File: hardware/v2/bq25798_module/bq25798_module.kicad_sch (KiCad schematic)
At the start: 54 parts, among them IC1 BQ25798RQMR, J1 Input 12V DC, J2 Output 12V DC, J3 Battery, J5 I2C (no pullups), J6 NTC temp sensor, Q1 AON7528, Q2 AON7528

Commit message: update board to v2.1
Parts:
- removed JP6: Temp simul, Jumper:SolderJumper-2_P1.3mm_Bridged_RoundedPad1.0x1.5mm, symbol Jumper:SolderJumper_2_Bridged
- removed NT3: ~, NetTie:NetTie-2_SMD_Pad0.5mm, symbol Device:NetTie_2
- removed TP1: TS, TestPoint:TestPoint_Loop_D1.80mm_Drill1.0mm_Beaded, symbol Connector:TestPoint
- added C23: 47n 25V, Capacitor_SMD:C_0402_1005Metric, symbol Device:C
- added D2: LED, LED_SMD:LED_1206_3216Metric, symbol Device:LED
- added J4: I2C, Connector_JST:JST_XH_B3B-XH-A_1x03_P2.50mm_Vertical, symbol Connector:Conn_01x03_Pin
- C1, C2: value 47n 10V -> 47n 25V; Parameters 10V X7R -> X7R; Source https://www.tme.eu/cz/details/grm155r71a473ka01d/kondenzato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 -> https://www.tme.eu/cz/details/gcm155r71e473ka55d/kondenzato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
- C10, C11, C12, C13, C14, C15, C16, C17, C18, C19, C21, C4: value 10u -> 10u 25V; Parameters 25V X5R -> X7R; Source https://www.tme.eu/cz/details/grm319r6ya106ka12d/kondenzato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 -> https://www.tme.eu/cz/details/grm31cr71e106ka12l/kondenzato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
- C20, C22, D1, L1: Bought basket @TME -> (none)
- C3: value 4.7u -> 4.7u 10V; footprint Capacitor_SMD:C_0805_2012Metric -> Capacitor_SMD:C_1206_3216Metric; Bought at home -> basket @TME; Parameters 25V X5R -> X7R; Source https://www.laskakit.cz/samsung-cl21a475kaqnnne-0805-4-7uf-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 -> https://www.tme.eu/cz/details/grm31cr71e106ka12l/kondenzato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; now fitted; now in the parts list
- C5, C6, C7, C9: value 100n -> 100n 25V; Parameters 50V X7R -> X7R; Source https://www.tme.eu/cz/details/c1005x7r1h104kbb/kondenzatory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 -> https://www.tme.eu/cz/details/gcm155r71e104ke02d/kondenzato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
- C8: value 1nF, 50V, 0402 package -> 1nF, 50V; Parameters 50V X7R -> X7R; Source https://www.tme.eu/cz/details/0402b102k500ct/kondenzatory-m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 -> https://www.tme.eu/cz/details/04023c102kat2a/kondenzatory-m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
- IC1: Bought bought @Ali -> bought @TI
- J5: value I2C (no pullups) -> I2C QWIIC/uŠup; Bought basket @TME -> (none)
- J6: footprint Connector_PinSocket_2.54mm:PinSocket_1x02_P2.54mm_Vertical -> Connector_JST:JST_XH_B2B-XH-A_1x02_P2.50mm_Vertical
- NT1: value grounds -> ~
- R1, R4, R5, R6, R7: Bought at home -> (none)
- R2: value 127k -> 1R; now fitted; now in the parts list
- R3: value 100k -> 1M; now fitted; now in the parts list
- R8: value ? -> 2k2; Bought (none) -> (none); now fitted
- R9: Parameters Do not populate if NTC is used -> (none)
- TP3: value GND -> PGND
- TP6: value Charge status (OD) -> STAT
- TP7: value Interrupt (OD) -> INT
- TP8: value REGN LDO -> REGN
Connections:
- net GND: now also J6.1 (Pin_1), J4.1 (Pin_1); no longer C8.2, IC1.10 (ACDRV2), IC1.13 (~{CE}), J6.2 (Pin_2), TP3.1
- net I2C_SCL: now also J4.3 (Pin_3)
- net I2C_SDA: now also J4.2 (Pin_2)
- net PGND: now also C8.2, IC1.10 (ACDRV2), TP3.1, C23.2
- net REGN: now also R6.1, R8.1
- net STAT: now also D2.1 (K)
- net TS: now also J6.2 (Pin_2); no longer J6.1 (Pin_1), R8.1, R9.2
- net at R8.2: now also D2.2 (A); no longer R6.1
- net at IC1.18 (BATP), R4.1: now also C23.1
- new net: IC1.13 (~{CE}), R9.2
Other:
- note added: "Controller connectors"
- note added: "Grounds"
- note added: "PGND = power ground (thicker traces, special net on PCB) GND = digital ground (ordinary traces) PWR_FLAGs are for DRC in PCB editor."
- note added: "RESET pin?"
- note removed: "255k = 500mA 127k = 1500 mA 0R = max current"
- note removed: "5,89 * REGN = normal temp"
- note removed: "Configure default switching frequency and cell count 27k = 750 kHz + 4 cells"
- note removed: "I2C connector"
- note removed: "Input current limit"
- note removed: "Simulate thermal state: 10k = normal 4.87k = warm 0R = hot"
- note removed: "Simulate thermal state: inf = normal 7.68k = cool 0R = cold"
- title: (none) -> BQ25798 UPS module
- moved on the sheet: C1, C10, C11, C12, C13, C14, C15, C16, C17, C18, C19, C2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

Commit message: wip
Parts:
- removed J5: I2C QWIIC/uŠup, Connector_JST:JST_SH_BM04B-SRSS-TB_1x04-1MP_P1.00mm_Vertical, symbol Connector:Conn_01x04_Pin
- added C24, C25: 47u low ESR, Capacitor_SMD:C_Elec_6.3x5.8, symbol Device:C_Polarized
- C10, C11, C12, C13, C14, C15, C16, C17, C18, C19, C21, C4: footprint Capacitor_SMD:C_1206_3216Metric -> Capacitor_SMD:C_0805_2012Metric; Source https://www.tme.eu/cz/details/grm31cr71e106ka12l/kondenzato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 -> https://www.tme.eu/cz/details/grj21br61e106ke01k/kondenzato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
- C23: Bought (none) -> basket @TME; Parameters 50V X7R -> X7R; Source https://www.tme.eu/cz/details/c1005x7r1h104kbb/kondenzatory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 -> https://www.tme.eu/cz/details/gcm155r71e473ka55d/kondenzato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
- C3: footprint Capacitor_SMD:C_1206_3216Metric -> Capacitor_SMD:C_0805_2012Metric; Source https://www.tme.eu/cz/details/grm31cr71e106ka12l/kondenzato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 -> https://www.tme.eu/cz/details/grm21br71e475ka73l/kondenzato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
- C8: Source https://www.tme.eu/cz/details/04023c102kat2a/kondenzatory-m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 -> https://www.tme.eu/cz/details/gcm1555c1h102ja16d/kondenzato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
- D1: Bought (none) -> ?? nemám je doma?
- D2, J4: Bought (none) -> at home
- L1: footprint snapeda:INDM7676X435N -> Inductor_SMD:L_12x12mm_H6mm; Bought (none) -> basket @TME; Parameters 7.06A I_sat -> >7.06A I_sat; Source https://www.tme.eu/cz/en/details/dr74-2r2-r/smd-power-induc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 -> https://www.tme.eu/cz/details/dr125-2r2-r/tlumivky/eaton-el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
- R3: Bought at home -> (none)
- R5: Parameters MEASURE CHECK!!! -> (none)
- R9: Bought at home -> basket @TME; Parameters (none) -> doplnění zásob; Source (none) -> https://www.tme.eu/cz/en/details/rt0805brd0710k/smd-resisto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
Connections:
- net PGND: now also C24.2, C25.2
- net PMID: now also C24.1, C25.1
- no-connect marks 4 -> 3
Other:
- note added: "?? nestacil by bezny?"
- moved on the sheet: J4

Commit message: v2.1 final
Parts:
- removed J4: I2C, Connector_JST:JST_XH_B3B-XH-A_1x03_P2.50mm_Vertical, symbol Connector:Conn_01x03_Pin
- removed TP6: STAT, TestPoint:TestPoint_Loop_D1.80mm_Drill1.0mm_Beaded, symbol Connector:TestPoint
- removed TP7: INT, TestPoint:TestPoint_Loop_D1.80mm_Drill1.0mm_Beaded, symbol Connector:TestPoint
- added J4: Controller Connection, Connector_JST:JST_XH_B6B-XH-A_1x06_P2.50mm_Vertical, symbol Connector:Conn_01x06_Pin
- added NT4: ~, NetTie:NetTie-2_SMD_Pad0.5mm, symbol Device:NetTie_2
- added TP1: GND, TestPoint:TestPoint_Loop_D1.80mm_Drill1.0mm_Beaded, symbol Connector:TestPoint
- C20, C22: now not fitted; now left out of the parts list
- D2: footprint LED_SMD:LED_1206_3216Metric -> LED_SMD:LED_0805_2012Metric; Bought at home -> basket @TME; Source (none) -> https://www.tme.eu/cz/details/597-3605-607f/diody-led-smd-b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
- J6: Source (none) -> https://www.tme.eu/cz/details/nrbe104f3380b1f/merici-termis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
- Q1, Q2: Bought (none) -> basket @TME; Source (none) -> https://www.tme.eu/cz/details/aon7528/tranzistory-s-kanalem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
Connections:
- net GND: now also IC1.10 (ACDRV2), J4.1 (Pin_1), TP1.1
- net PGND: no longer IC1.10 (ACDRV2)
- net at IC1.13 (~{CE}), R9.2: now also J4.5 (Pin_5)
- net at Q2.5 (D), Q2.6 (D), Q2.7 (D)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: now also NT4.2; no longer IC1.2 (VBUS_1), IC1.3 (VBUS_2), IC1.8 (VAC2)
- net I2C_SCL: no longer names the net of IC1.14 (SCL)
- net I2C_SCL: now also J4.3 (Pin_3)
- net I2C_SDA: no longer names the net of IC1.15 (SDA)
- net I2C_SDA: now also J4.2 (Pin_2)
- net ~{INT}: no longer names the net of IC1.21 (~{INT})
- net ~{INT}: now also J4.6 (Pin_6)
- new net: IC1.2 (VBUS_1), IC1.3 (VBUS_2), IC1.8 (VAC2), NT4.1
- no-connect marks 3 -> 4
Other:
- note removed: "?? nestacil by bezny?"
- note removed: "Controller connectors"
- note removed: "RESET pin?"
- moved on the sheet: C3, D2, J6, R2, R3, R6, R7, R8, R9

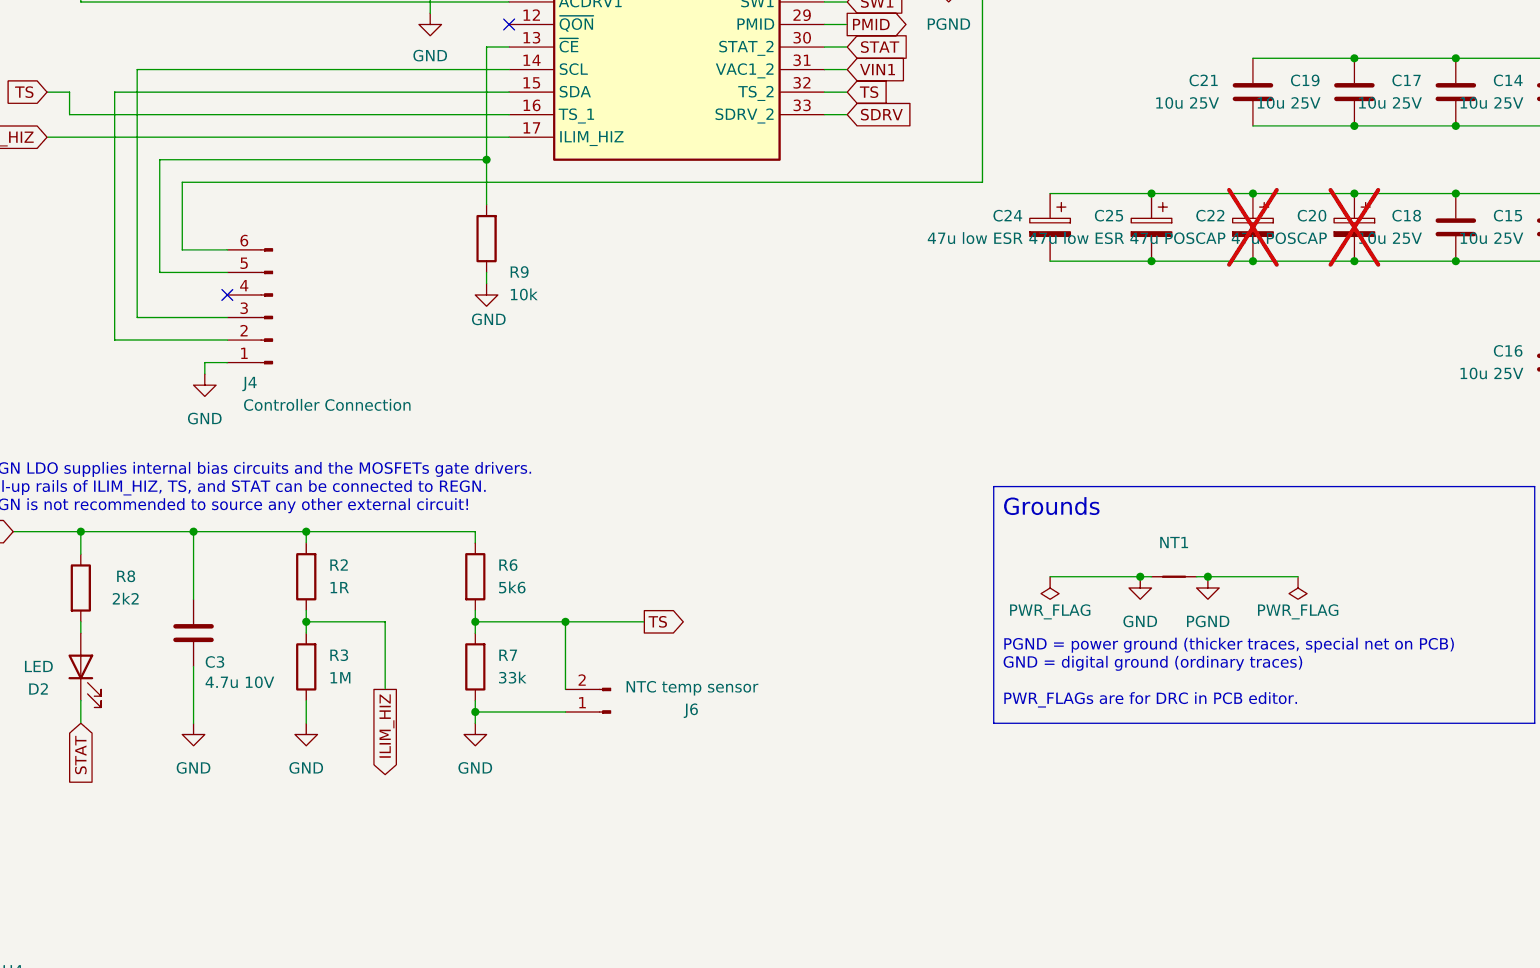
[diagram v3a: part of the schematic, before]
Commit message: add thermal reliefs, simplify PCB
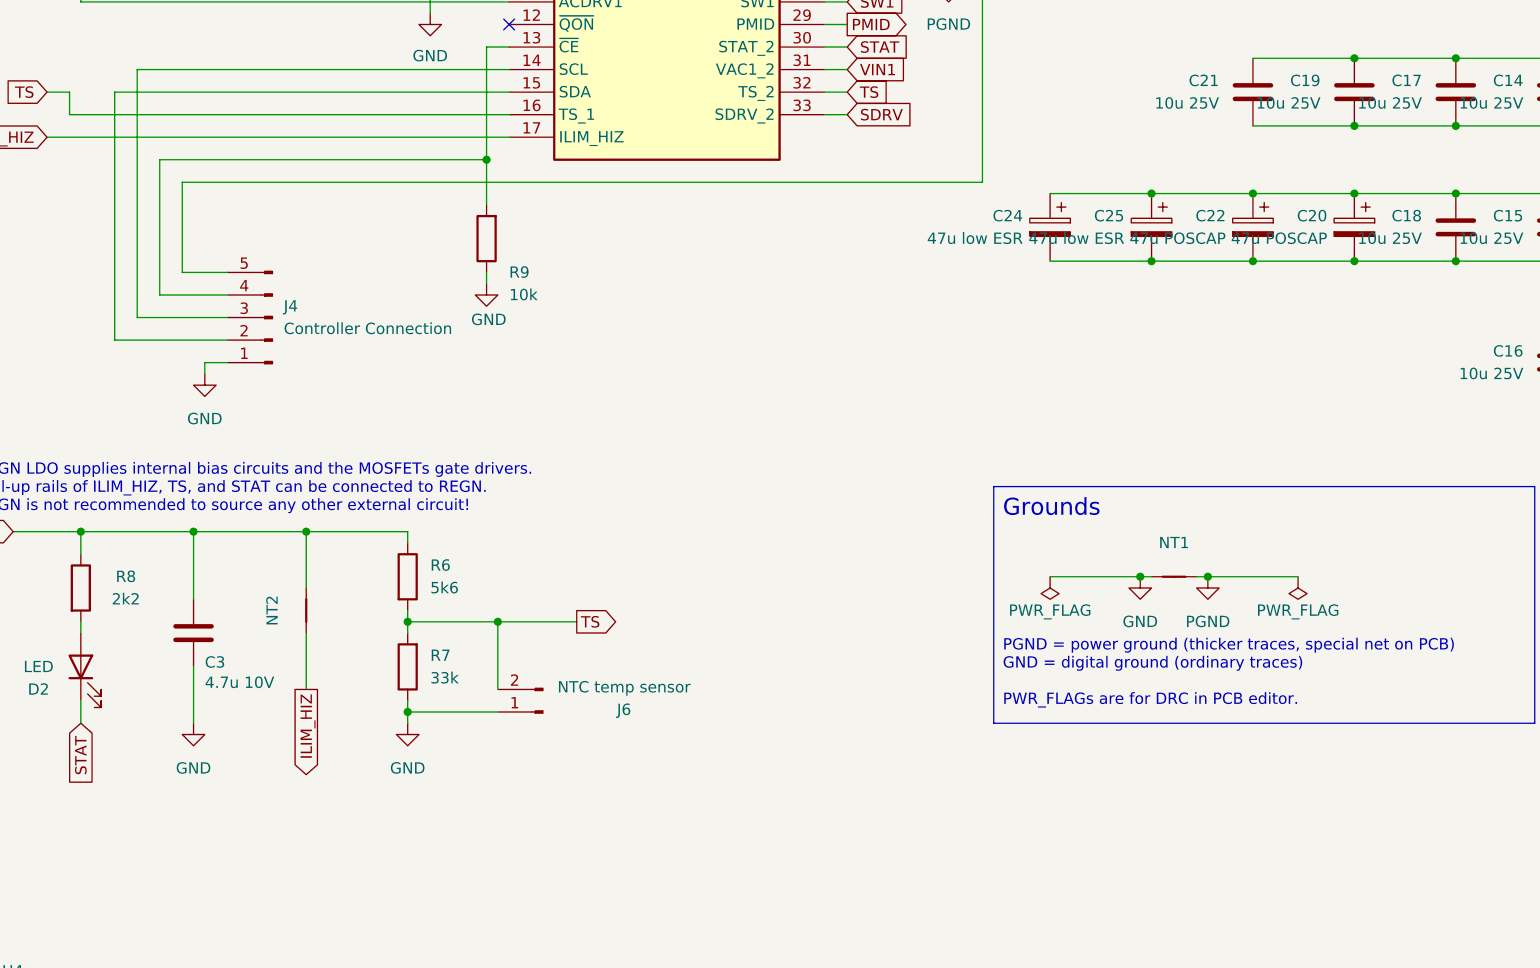
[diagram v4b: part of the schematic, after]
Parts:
- removed J4: Controller Connection, Connector_JST:JST_XH_B6B-XH-A_1x06_P2.50mm_Vertical, symbol Connector:Conn_01x06_Pin
- removed R2: 1R, Resistor_SMD:R_0805_2012Metric, symbol Device:R
- removed R3: 1M, Resistor_SMD:R_0805_2012Metric, symbol Device:R
- added J4: Controller Connection, Connector_JST:JST_XH_B5B-XH-A_1x05_P2.50mm_Vertical, symbol Connector:Conn_01x05_Pin
- added NT2: ~, NetTie:NetTie-2_SMD_Pad0.5mm, symbol Device:NetTie_2
- C20, C22: now fitted; now in the parts list
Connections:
- net GND: now also J4.1 (Pin_1)
- net ILIM_HIZ: now also NT2.1
- net REGN: now also NT2.2
- net at IC1.13 (~{CE}), R9.2: now also J4.4 (Pin_4)
- net at IC1.15 (SDA): now also J4.2 (Pin_2)
- net at IC1.14 (SCL): now also J4.3 (Pin_3)
- net at IC1.21 (~{INT}): now also J4.5 (Pin_5)
- no-connect marks 4 -> 3
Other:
- moved on the sheet: J6, R6, R7

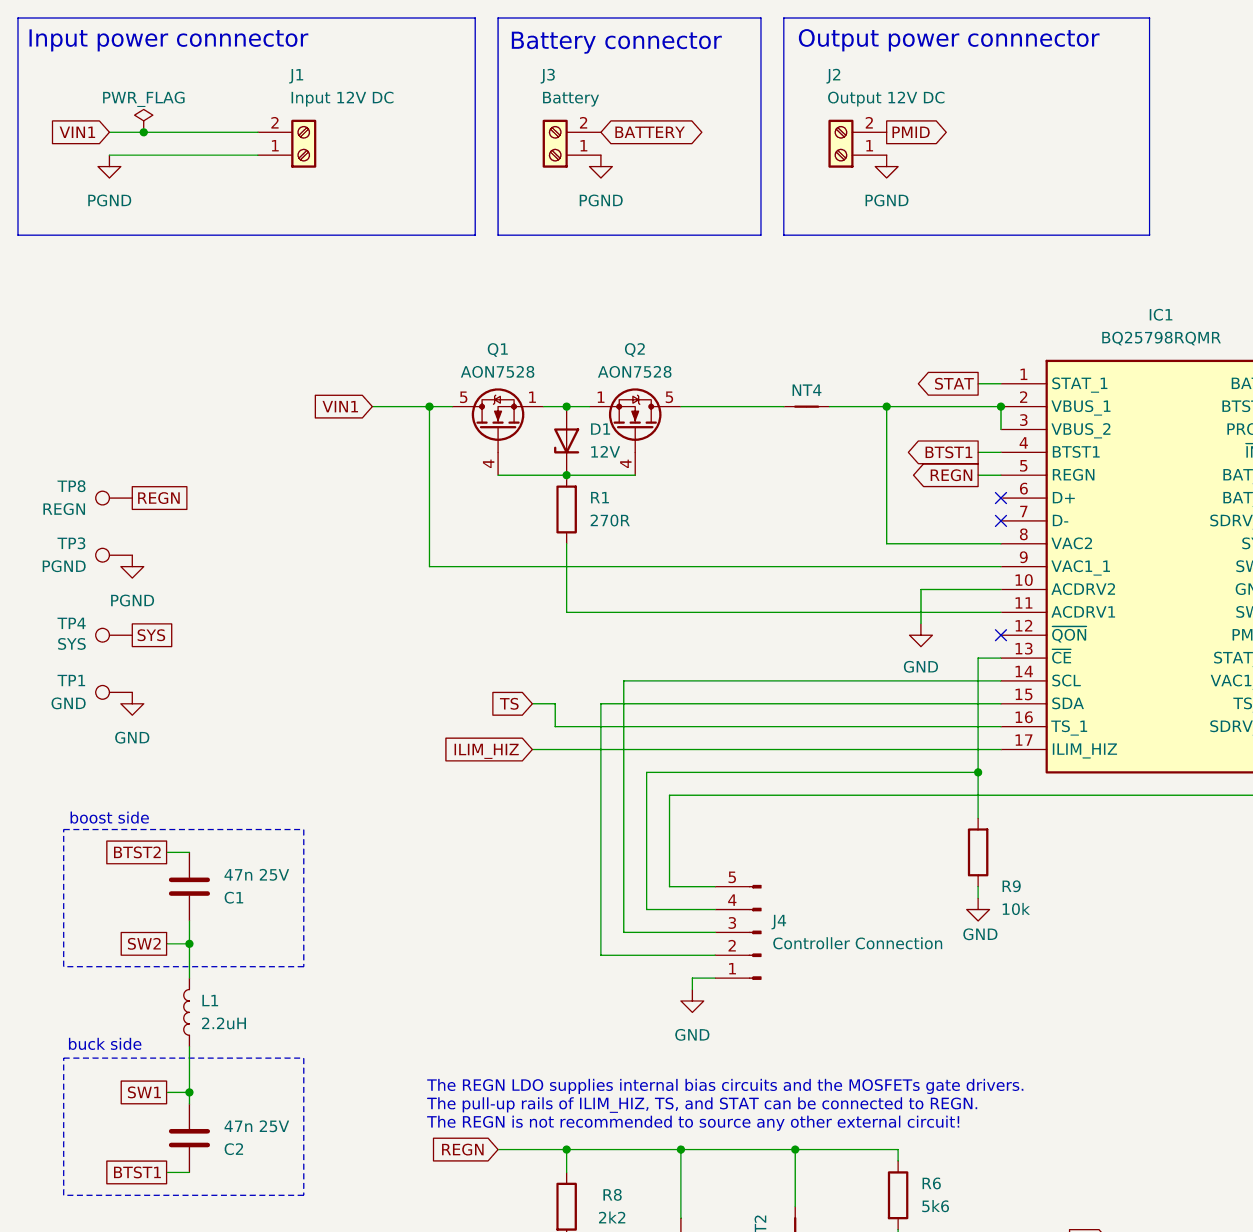
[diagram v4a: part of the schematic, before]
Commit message: add power output to the J4
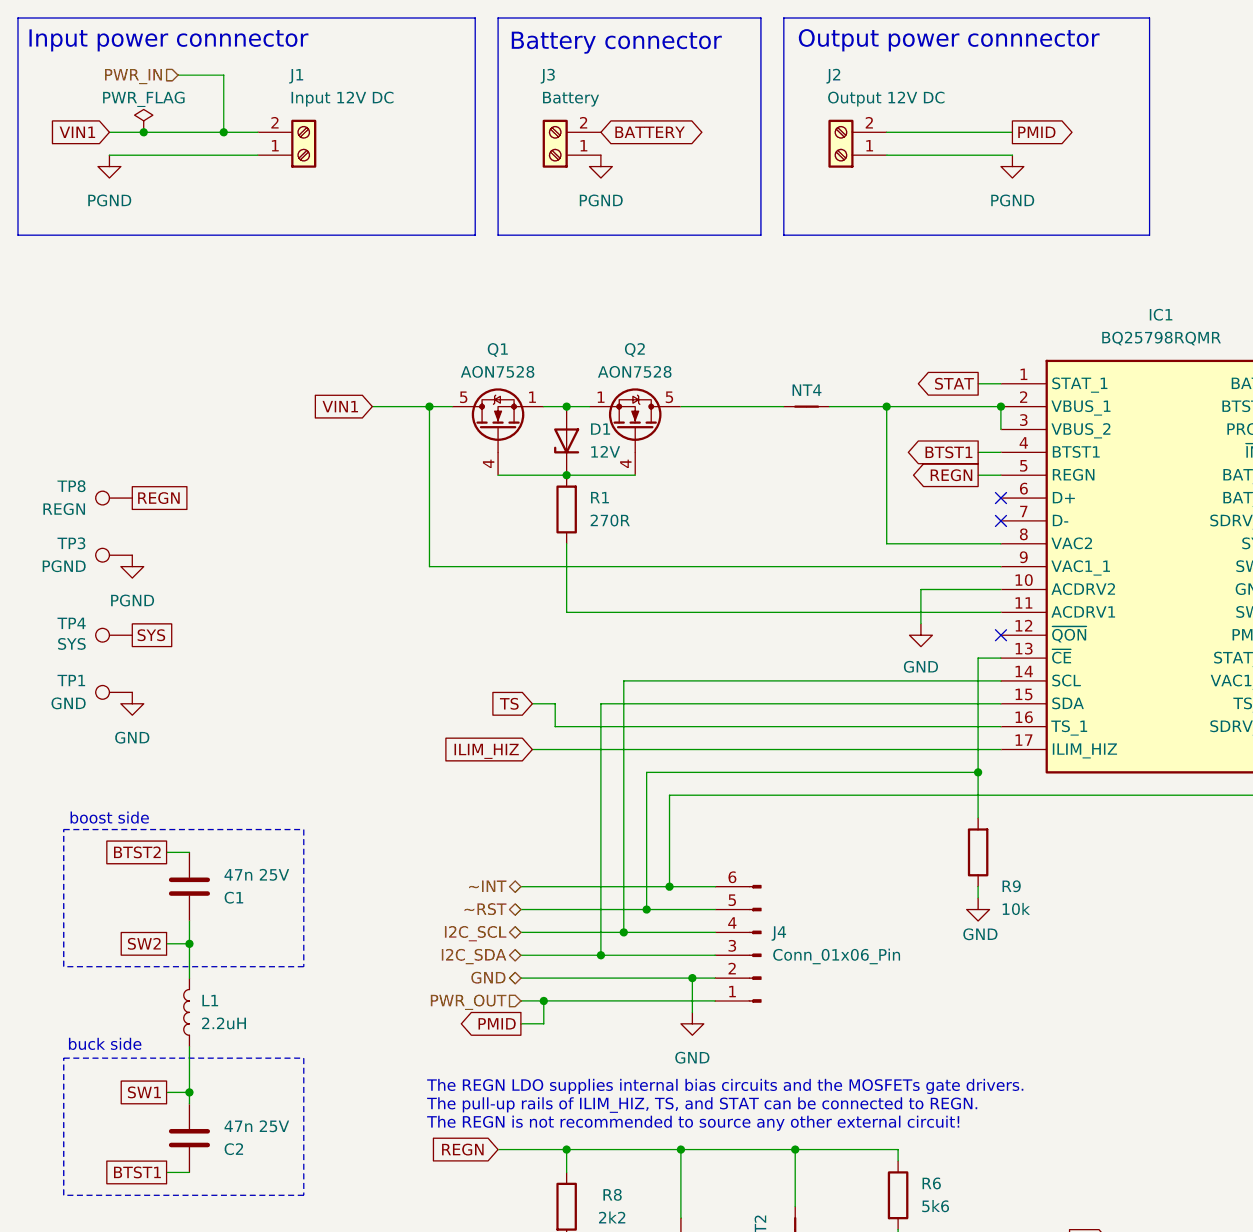
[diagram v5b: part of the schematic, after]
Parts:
- removed J4: Controller Connection, Connector_JST:JST_XH_B5B-XH-A_1x05_P2.50mm_Vertical, symbol Connector:Conn_01x05_Pin
- added J4: Conn_01x06_Pin, Connector_JST:JST_XH_B6B-XH-A_1x06_P2.50mm_Vertical, symbol Connector:Conn_01x06_Pin
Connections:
- net GND: now also J4.2 (Pin_2)
- net PMID: now also J4.1 (Pin_1)
- net ~RST: now reaches IC1.13 (~{CE}), R9.2
- net ~RST: now also J4.5 (Pin_5)
- net I2C_SDA: now reaches IC1.15 (SDA)
- net I2C_SDA: now also J4.3 (Pin_3)
- net I2C_SCL: now reaches IC1.14 (SCL)
- net I2C_SCL: now also J4.4 (Pin_4)
- net ~INT: now reaches IC1.21 (~{INT})
- net ~INT: now also J4.6 (Pin_6)
